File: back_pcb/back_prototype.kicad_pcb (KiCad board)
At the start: 2 copper layers, 40 x 100 mm, 84 parts, among them P1 EXPANSION_LEFT, P2 EXPANSION_BOTTOM, P3 EXPANSION_TOP, P4 USB_A, P5 AUDIO_CONN, P6 ATMEGA_HEADER, P7 EXPANSION_BOTTOM2, P8 CONN_01X02, Q1 IRLML6401, Q2 BSS138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

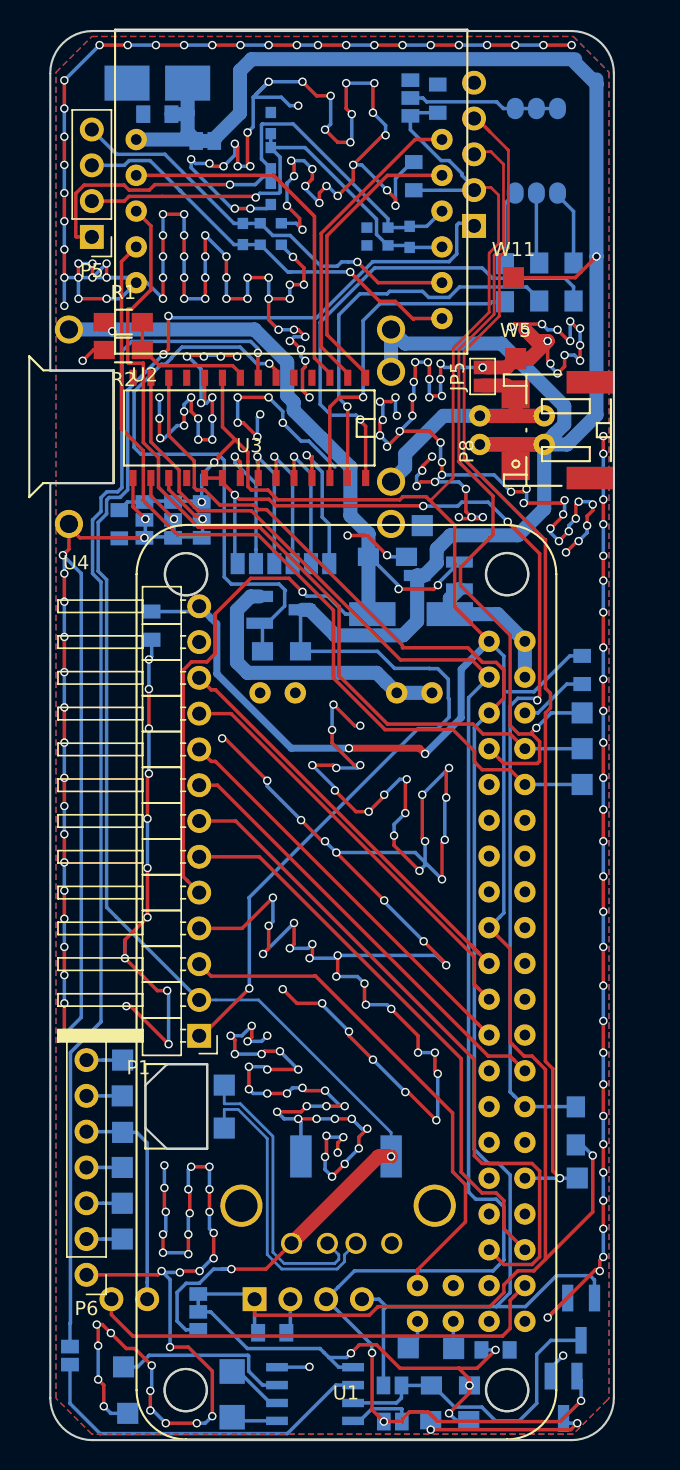
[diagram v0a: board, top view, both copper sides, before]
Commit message: Back board almost finished - lots of changes
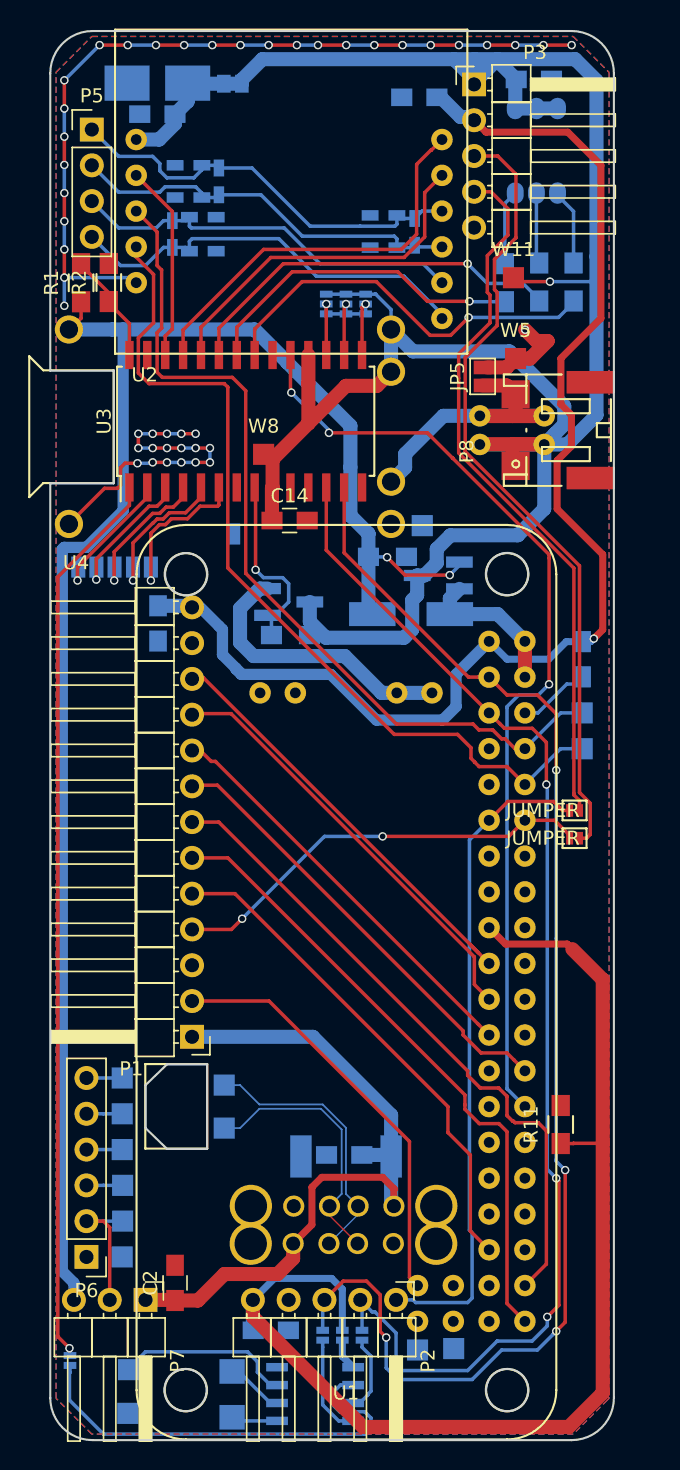
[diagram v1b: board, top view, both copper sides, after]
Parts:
- removed C7: 100nF, Capacitors_SMD:C_0805
- removed JP8: CA/CC, Connect:GS3
- removed Q2, Q3: BSS138, TO_SOT_Packages_SMD:SOT-23_Handsoldering
- removed R8, R9: 10K, Resistors_SMD:R_0805_HandSoldering
- removed W16: TEST_1P, Measurement_Points:Measurement_Point_Square-SMD-Pad_Small
- added C1: 100nF, Capacitors_SMD:C_0805_HandSoldering, B.Cu at (62.4, 119.8)
- added C2: 100nF, Capacitors_SMD:C_0805_HandSoldering, F.Cu at (50.4, 128.8)
- added JP11: JUMPER, common-footprints:GS2_SMALL, F.Cu at (79.1, 95.3)
- added JP12: JUMPER, common-footprints:GS2_SMALL, F.Cu at (79.1, 97.3)
- added P9: USB_A, footprints:USB_A, B.Cu at (65.9, 123.4)
- C13, C15, C25, C5, C6, C8: footprint Capacitors_SMD:C_0805 -> Capacitors_SMD:C_0805_HandSoldering
- C14: footprint Capacitors_SMD:C_0805 -> Capacitors_SMD:C_0805_HandSoldering; moved to F.Cu
- C16, C17, C18, C19, C20, C21, C22, C23, C24: footprint Capacitors_SMD:C_0603 -> Capacitors_SMD:C_0603_HandSoldering
- C4: value 10uF -> 100uF
- JP10, JP2, JP9: footprint Connect:GS2 -> common-footprints:GS2_SMALL
- JP3, JP4, JP6: footprint Connect:GS3 -> common-footprints:GS3_SMALL
- JP7: value 3V3/5V -> Jumper_NC_Small; footprint Connect:GS3 -> common-footprints:GS2_SMALL
- P2: footprint Pin_Headers:Pin_Header_Angled_1x04_Pitch2.54mm -> Pin_Headers:Pin_Header_Angled_1x05_Pitch2.54mm; moved to F.Cu
- P3, R11, W8: moved to F.Cu
- P4: footprint Connect:USB_A -> footprints:USB_A
- P6: footprint Pin_Headers:Pin_Header_Straight_1x07_Pitch2.54mm -> Pin_Headers:Pin_Header_Straight_1x06_Pitch2.54mm
- P7: footprint Pin_Headers:Pin_Header_Angled_1x02_Pitch2.54mm -> Pin_Headers:Pin_Header_Angled_1x03_Pitch2.54mm; moved to F.Cu
- P8: value CONN_01X02 -> JST
- U3: footprint SMD_Packages:SOIC-28 -> Housings_SOIC:SOIC-28W_7.5x17.9mm_Pitch1.27mm
- W12, W5, W6: value TEST_1P -> GND
- W27: value TEST_1P -> ATMEGA_VCC
- moved W7 52.9 mm to (48.6, 78.0), turned to 90 degrees
- moved W6 50.6 mm to (46.6, 127.0)
- moved W8 46.6 mm to (56.6, 70.0)
- moved JP3 21.9 mm to (63.9, 59.4)
- moved JP6 19.6 mm to (62.5, 59.4)
- moved JP4 17.7 mm to (61.1, 59.4)
- moved W23 12.6 mm to (47.6, 78.0)
- moved W24 12.6 mm to (49.2, 78.0)
- moved W22 12.6 mm to (46.0, 78.0)
- moved W21 12.6 mm to (44.4, 78.0)
- moved C14 12.1 mm to (58.5, 74.7), turned to 0 degrees
- moved W13 11.4 mm to (46.6, 114.3)
- moved JP7 10.3 mm to (62.2, 132.2), turned to 0 degrees
- moved P3 10.0 mm to (71.6, 43.8)
- moved P2 10.0 mm to (66.0, 130.0)
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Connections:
- C13 pad 1: +3V3 -> +BATT
- C14 pad 1: +3V3 -> +BATT
- C16 pad 2: MIC+ -> MIC-
- C17 pad 1: MIC+ -> MIC-
- C17 pad 2: MIC- -> MIC+
- C18 pad 1: MIC- -> MIC+
- C19 pad 2: SPK+ -> SPK-
- C20 pad 1: SPK+ -> SPK-
- C20 pad 2: SPK- -> SPK+
- C21 pad 1: SPK- -> SPK+
- C22 pad 2: MIC+ -> MIC-
- C23 pad 1: MIC+ -> MIC-
- C23 pad 2: MIC- -> MIC+
- C24 pad 1: MIC- -> MIC+
- D3 pad 1: Net-(D3-Pad1) -> +BATT
- JP2 pad 1: RTC_ALARM -> Net-(JP2-Pad1)
- JP2 pad 2: Net-(JP2-Pad2) -> RTC_ALARM
- JP3 pad 3: +3V3 -> +BATT
- JP4 pad 1: +3V3 -> +BATT
- JP6 pad 3: +3V3 -> +BATT
- JP7 pad 1: +3V3 -> Net-(JP7-Pad1)
- P1 pad 1: +BATT -> +5V
- P1 pad 2: +5V -> TV_OUT
- P1 pad 3: TV_OUT -> GND
- P1 pad 4: GND -> LH_GPIO_4
- P1 pad 5: VDD -> LH_GPIO_3
- P2 pad 1: +3V3 -> BH_GPIO_1
- P2 pad 2: GND -> SCL
- P2 pad 4: SCL -> GND
- P3 pad 1: +5V -> +BATT
- P5 pad 3: SPK- -> SPK+
- P5 pad 4: SPK+ -> SPK-
- P6 pad 2: ATMEGA_RST -> ATMEGA_ADC
- P6 pad 3: ATMEGA_RXD -> Net-(P6-Pad3)
- P6 pad 4: ATMEGA_TXD -> ATMEGA_RXD
- P6 pad 5: ATMEGA_ADC -> ATMEGA_TXD
- P6 pad 6: ATMEGA_GPIO -> ATMEGA_R_G
- P7 pad 1: BH_GPIO -> +5V
- U1 pad 11: (no net) -> BH_GPIO_1
- U1 pad 12: (no net) -> LH_GPIO_4
- U1 pad 32: IR_RX -> (no net)
- U1 pad 35: LH_GPIO_1 -> LH_GPIO_3
- U1 pad 36: LH_GPIO_2 -> (no net)
- U1 pad 38: BH_GPIO -> LH_GPIO_1
- U1 pad 40: (no net) -> LH_GPIO_2
- U1 pad 44: Net-(U1-Pad44) -> GND
- U1 pad 7: IR_TX -> (no net)
- U3 pad 1: SIM800_DTR -> RTC_ALARM
- U3 pad 18: (no net) -> +BATT
- U3 pad 2: SIM800_RING -> Net-(U3-Pad2)
- U3 pad 21: Net-(U3-Pad21) -> NOTIF_LED_R
- U3 pad 22: Net-(U3-Pad22) -> NOTIF_LED_B
- U3 pad 23: Net-(U3-Pad23) -> NOTIF_LED_G
- U3 pad 24: Net-(U3-Pad24) -> SIM800_DTR
- U3 pad 25: Net-(U3-Pad25) -> SIM800_RING
- U3 pad 26: NOTIF_LED_B -> SIM800_RST
- U3 pad 27: NOTIF_LED_G -> (no net)
- U3 pad 28: NOTIF_LED_R -> CHARGING_SENSE
- U3 pad 3: SIM800_RST -> Net-(U3-Pad3)
- U3 pad 4: (no net) -> Net-(U3-Pad4)
- U3 pad 5: (no net) -> Net-(U3-Pad5)
- U3 pad 6: DCDC_EN -> Net-(U3-Pad6)
- U3 pad 7: Net-(JP2-Pad2) -> Net-(U3-Pad7)
- U3 pad 8: CHARGING_SENSE -> DCDC_EN
- U3 pad 9: +3V3 -> +BATT
- U5 pad 5: +3V3 -> Net-(JP7-Pad1)
- U5 pad 6: RTC_ALARM -> Net-(JP2-Pad1)
- W13 pad 1: ATMEGA_RST -> ATMEGA_R_G
- W21 pad 1: Net-(U3-Pad21) -> Net-(U3-Pad2)
- W22 pad 1: Net-(U3-Pad22) -> Net-(U3-Pad3)
- W23 pad 1: Net-(U3-Pad23) -> Net-(U3-Pad4)
- W24 pad 1: Net-(U3-Pad24) -> Net-(U3-Pad5)
- W27 pad 1: Net-(P6-Pad7) -> Net-(P6-Pad3)
- W4 pad 1: Net-(U1-Pad44) -> GND
- W6 pad 1: IR_TX -> GND
- W7 pad 1: IR_RX -> Net-(U3-Pad6)
- W8 pad 1: ATMEGA_GPIO -> Net-(U3-Pad7)
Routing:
- net GND: track 778.0 -> 110.4 mm, vias 346 -> 48
- net Net-(JP2-Pad2): track 85.4 -> 0.00 mm, vias 1 -> 0
- net +3V3: track 249.1 -> 176.0 mm, vias 9 -> 1
- net +5V: track 122.6 -> 50.4 mm, vias 4 -> 0
- net BH_GPIO_1: track 0.00 -> 46.7 mm
- net RTC_ALARM: track 25.2 -> 64.1 mm, vias 0 -> 1
- net VDD: track 83.2 -> 120.2 mm, vias 4 -> 2
- net LH_GPIO_3: track 0.00 -> 35.8 mm
- net BH_GPIO: track 33.7 -> 0.00 mm
- net IR_RX: track 84.2 -> 50.8 mm, vias 1 -> 0
- net Net-(JP2-Pad1): track 0.00 -> 31.3 mm
- net LH_GPIO_4: track 0.00 -> 30.6 mm, vias 0 -> 2
- net DCDC_EN: track 42.0 -> 13.3 mm
- net SDA: track 121.5 -> 95.1 mm, vias 3 -> 4
- net SCL: track 108.6 -> 88.3 mm, vias 0 -> 3
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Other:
- net class Default: trace_width 0.1 -> 0.25

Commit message: Cleaning up ground planes
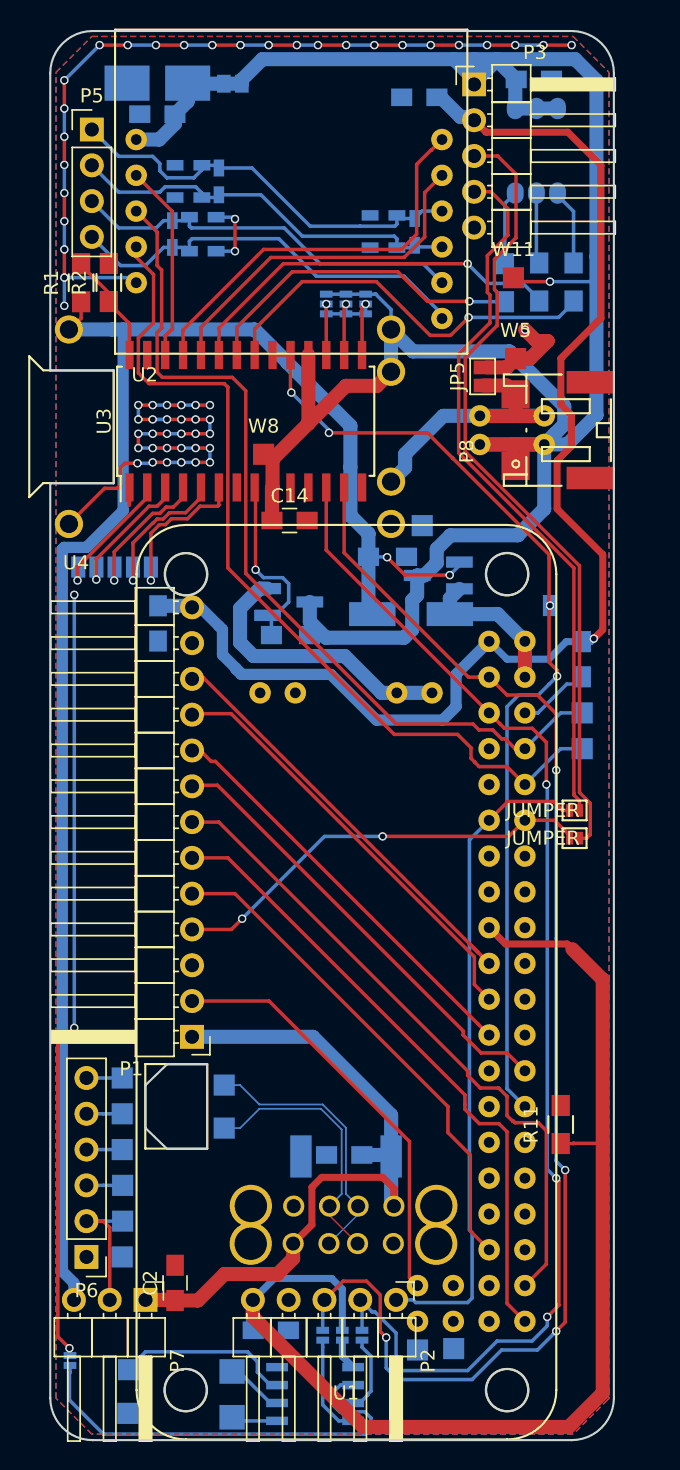
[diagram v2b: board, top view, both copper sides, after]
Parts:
- moved W28 23.0 mm to (77.6, 80.8)
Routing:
- net GND: track 110.4 -> 128.7 mm, vias 48 -> 63
- net RTC_ALARM: track 64.1 -> 56.1 mm, vias 1 -> 3
- net Net-(U3-Pad7): track 0.00 -> 5.59 mm
- net +BATT: track 171.6 -> 166.0 mm
- net MCP_INT: track 68.9 -> 69.6 mm, vias 3 -> 4
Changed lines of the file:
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@@
   (general
     (links 196)
-    (no_connects 18)
+    (no_connects 13)
     (area 41.424999 39.924999 81.575001 140.075001)
     (thickness 1.6)
     (drawings 22)
-    (tracks 832)
+    (tracks 875)
     (zones 0)
     (modules 82)
@@
     (36 B.SilkS user hide)
     (37 F.SilkS user hide)
-    (38 B.Mask user hide)
-    (39 F.Mask user hide)
+    (38 B.Mask user)
+    (39 F.Mask user)
     (40 Dwgs.User user hide)
     (41 Cmts.User user hide)
@@
   )
   (module Measurement_Points:Measurement_Point_Square-SMD-Pad_Small (layer B.Cu)
-    (at 55.083 75.692)
+    (at 77.562 80.772)
     (descr "Mesurement Point, Square, SMD Pad,  1.5mm x 1.5mm,")
     (tags "Mesurement Point Square SMD Pad 1.5x1.5mm")
@@
   (segment (start 70.612 46.101) (end 71.3486 46.101) (width 1) (layer B.Cu) (net 1))
   (segment (start 51.6928 81.2) (end 52.07 80.8228) (width 0.25) (layer B.Cu) (net 1))
+  (segment (start 51.816 66.548) (end 52.832 66.548) (width 0.25) (layer F.Cu) (net 2))
+  (via (at 52.832 66.548) (size 0.6) (drill 0.4) (layers F.Cu B.Cu) (net 2))
+  (segment (start 50.8 66.548) (end 51.816 66.548) (width 0.25) (layer B.Cu) (net 2))
+  (via (at 51.816 66.548) (size 0.6) (drill 0.4) (layers F.Cu B.Cu) (net 2))
+  (segment (start 49.784 66.548) (end 50.8 66.548) (width 0.25) (layer F.Cu) (net 2))
+  (via (at 50.8 66.548) (size 0.6) (drill 0.4) (layers F.Cu B.Cu) (net 2))
+  (segment (start 48.768 66.548) (end 49.784 66.548) (width 0.25) (layer B.Cu) (net 2))
+  (via (at 49.784 66.548) (size 0.6) (drill 0.4) (layers F.Cu B.Cu) (net 2))
+  (segment (start 47.752 66.548) (end 48.768 66.548) (width 0.25) (layer F.Cu) (net 2))
+  (via (at 48.768 66.548) (size 0.6) (drill 0.4) (layers F.Cu B.Cu) (net 2))
+  (segment (start 47.752 67.564) (end 47.752 66.548) (width 0.25) (layer B.Cu) (net 2))
+  (via (at 47.752 66.548) (size 0.6) (drill 0.4) (layers F.Cu B.Cu) (net 2))
+  (segment (start 48.768 67.564) (end 47.752 67.564) (width 0.25) (layer F.Cu) (net 2))
+  (via (at 47.752 67.564) (size 0.6) (drill 0.4) (layers F.Cu B.Cu) (net 2))
+  (segment (start 49.784 67.564) (end 48.768 67.564) (width 0.25) (layer B.Cu) (net 2))
+  (via (at 48.768 67.564) (size 0.6) (drill 0.4) (layers F.Cu B.Cu) (net 2))
+  (segment (start 50.8 67.564) (end 49.784 67.564) (width 0.25) (layer F.Cu) (net 2))
+  (via (at 49.784 67.564) (size 0.6) (drill 0.4) (layers F.Cu B.Cu) (net 2))
+  (via (at 50.8 67.564) (size 0.6) (drill 0.4) (layers F.Cu B.Cu) (net 2))
+  (segment (start 51.816 67.564) (end 50.8 67.564) (width 0.25) (layer F.Cu) (net 2))
+  (via (at 51.816 67.564) (size 0.6) (drill 0.4) (layers F.Cu B.Cu) (net 2))
+  (segment (start 52.832 67.564) (end 51.816 67.564) (width 0.25) (layer F.Cu) (net 2))
+  (segment (start 52.832 68.58) (end 52.832 67.564) (width 0.25) (layer B.Cu) (net 2))
+  (via (at 52.832 67.564) (size 0.6) (drill 0.4) (layers F.Cu B.Cu) (net 2))
+  (segment (start 51.816 68.58) (end 52.832 68.58) (width 0.25) (layer F.Cu) (net 2))
+  (via (at 52.832 68.58) (size 0.6) (drill 0.4) (layers F.Cu B.Cu) (net 2))
+  (segment (start 54.61 55.626) (end 53.274 55.626) (width 0.25) (layer B.Cu) (net 2))
+  (segment (start 54.61 53.34) (end 54.61 55.626) (width 0.25) (layer F.Cu) (net 2))
+  (via (at 54.61 55.626) (size 0.6) (drill 0.4) (layers F.Cu B.Cu) (net 2))
+  (segment (start 53.274 53.213) (end 54.483 53.213) (width 0.25) (layer B.Cu) (net 2))
+  (segment (start 54.483 53.213) (end 54.61 53.34) (width 0.25) (layer B.Cu) (net 2))
+  (via (at 54.61 53.34) (size 0.6) (drill 0.4) (layers F.Cu B.Cu) (net 2))
   (segment (start 50.8 68.58) (end 51.816 68.58) (width 0.25) (layer F.Cu) (net 2))
   (via (at 51.816 68.58) (size 0.6) (drill 0.4) (layers F.Cu B.Cu) (net 2))
@@
   (segment (start 64.684401 65.180799) (end 62.488201 65.180799) (width 1) (layer F.Cu) (net 16))
   (segment (start 62.488201 65.180799) (end 59.817 67.852) (width 1) (layer F.Cu) (net 16))
-  (segment (start 57.277 72.392) (end 57.277 70.392) (width 1) (layer F.Cu) (net 16))
-  (segment (start 57.277 70.392) (end 59.817 67.852) (width 1) (layer F.Cu) (net 16))
   (segment (start 59.817 67.852) (end 59.817 64.992) (width 1) (layer F.Cu) (net 16))
   (segment (start 59.817 64.992) (end 59.817 62.992) (width 1) (layer F.Cu) (net 16))
@@
   (segment (start 71.9836 69.342) (end 76.5556 69.342) (width 1) (layer B.Cu) (net 16))
   (segment (start 65.6844 61.1808) (end 65.6844 64.1808) (width 1) (layer B.Cu) (net 16))
+  (segment (start 43.2045 110.744) (end 43.2045 80.01) (width 0.25) (layer B.Cu) (net 17))
+  (via (at 43.2045 80.01) (size 0.6) (drill 0.4) (layers F.Cu B.Cu) (net 17))
+  (segment (start 42.037 112.014) (end 42.037 132.6515) (width 0.25) (layer F.Cu) (net 17))
+  (segment (start 42.037 112.014) (end 42.037 111.9115) (width 0.25) (layer F.Cu) (net 17))
+  (segment (start 42.037 111.9115) (end 43.2045 110.744) (width 0.25) (layer F.Cu) (net 17))
+  (via (at 43.2045 110.744) (size 0.6) (drill 0.4) (layers F.Cu B.Cu) (net 17))
   (segment (start 42.8625 133.477) (end 42.8625 133.9625) (width 0.25) (layer B.Cu) (net 17))
   (segment (start 42.8625 133.9625) (end 42.9 134) (width 0.25) (layer B.Cu) (net 17))
-  (segment (start 42.037 78.74) (end 42.037 132.6515) (width 0.25) (layer F.Cu) (net 17))
   (segment (start 42.037 132.6515) (end 42.8625 133.477) (width 0.25) (layer F.Cu) (net 17))
   (via (at 42.8625 133.477) (size 0.6) (drill 0.4) (layers F.Cu B.Cu) (net 17))
-  (segment (start 47.117 73.66) (end 42.037 78.74) (width 0.25) (layer F.Cu) (net 17))
   (segment (start 47.117 73.092) (end 47.117 73.66) (width 0.25) (layer F.Cu) (net 17))
   (segment (start 47.117 72.392) (end 47.117 73.092) (width 0.25) (layer F.Cu) (net 17))
@@
   (segment (start 75.184 93.472) (end 77.724 90.932) (width 0.25) (layer B.Cu) (net 37))
   (segment (start 77.724 90.932) (end 79.248 90.932) (width 0.25) (layer B.Cu) (net 37))
+  (segment (start 76.8985 84.792736) (end 76.8985 84.7725) (width 0.25) (layer F.Cu) (net 38))
+  (segment (start 76.8985 84.7725) (end 76.8985 81.026) (width 0.25) (layer F.Cu) (net 38))
+  (segment (start 77.47 85.7885) (end 77.47 85.364236) (width 0.25) (layer F.Cu) (net 38))
+  (segment (start 77.47 85.364236) (end 76.8985 84.792736) (width 0.25) (layer F.Cu) (net 38))
+  (segment (start 76.8985 86.36) (end 77.47 85.7885) (width 0.25) (layer B.Cu) (net 38))
+  (via (at 77.47 85.7885) (size 0.6) (drill 0.4) (layers F.Cu B.Cu) (net 38))
+  (segment (start 73.914 87.9475) (end 74.7395 87.122) (width 0.25) (layer B.Cu) (net 38))
+  (segment (start 75.184 116.332) (end 73.914 115.062) (width 0.25) (layer B.Cu) (net 38))
+  (segment (start 73.914 115.062) (end 73.914 87.9475) (width 0.25) (layer B.Cu) (net 38))
+  (segment (start 76.1365 87.122) (end 76.8985 86.36) (width 0.25) (layer B.Cu) (net 38))
+  (segment (start 74.7395 87.122) (end 76.1365 87.122) (width 0.25) (layer B.Cu) (net 38))
+  (segment (start 76.8985 81.026) (end 76.8985 77.4065) (width 0.25) (layer F.Cu) (net 38))
+  (segment (start 76.962 80.772) (end 76.962 80.9625) (width 0.25) (layer F.Cu) (net 38))
+  (segment (start 76.962 80.9625) (end 76.8985 81.026) (width 0.25) (layer F.Cu) (net 38))
+  (via (at 76.962 80.772) (size 0.6) (drill 0.4) (layers F.Cu B.Cu) (net 38))
   (segment (start 61.2775 68.5165) (end 68.2625 68.5165) (width 0.25) (layer F.Cu) (net 38))
   (segment (start 68.2625 68.5165) (end 70.0405 70.2945) (width 0.25) (layer F.Cu) (net 38))
@@
   (segment (start 76.8985 77.1525) (end 70.08499 70.33899) (width 0.25) (layer F.Cu) (net 38))
   (segment (start 76.8985 77.4065) (end 76.8985 77.1525) (width 0.25) (layer F.Cu) (net 38))
-  (segment (start 74.7395 87.122) (end 76.1365 87.122) (width 0.25) (layer B.Cu) (net 38))
-  (segment (start 76.1365 87.122) (end 76.8985 86.36) (width 0.25) (layer B.Cu) (net 38))
-  (via (at 76.8985 86.36) (size 0.6) (drill 0.4) (layers F.Cu B.Cu) (net 38))
-  (segment (start 73.914 115.062) (end 73.914 88.011) (width 0.25) (layer B.Cu) (net 38))
-  (segment (start 73.914 88.011) (end 73.914 87.9475) (width 0.25) (layer B.Cu) (net 38))
-  (segment (start 73.914 87.9475) (end 74.7395 87.122) (width 0.25) (layer B.Cu) (net 38))
-  (segment (start 75.184 116.332) (end 73.914 115.062) (width 0.25) (layer B.Cu) (net 38))
-  (segment (start 76.8985 86.36) (end 76.8985 77.4065) (width 0.25) (layer F.Cu) (net 38))
   (segment (start 57.277 62.992) (end 58.547 62.992) (width 0.25) (layer F.Cu) (net 38))
   (segment (start 57.592 138.6332) (end 54.662 138.6332) (width 0.25) (layer B.Cu) (net 39))
@@
   (segment (start 53.467 72.392) (end 53.467 73.642) (width 0.25) (layer F.Cu) (net 60))
   (segment (start 53.467 73.642) (end 53.3855 73.7235) (width 0.25) (layer F.Cu) (net 60))
+  (segment (start 57.277 72.392) (end 57.277 70.392) (width 1) (layer F.Cu) (net 61))
+  (segment (start 57.277 70.392) (end 59.817 67.852) (width 1) (layer F.Cu) (net 61))
   (segment (start 66.04 130.048) (end 67.242081 130.048) (width 0.25) (layer B.Cu) (net 62))
   (segment (start 67.242081 130.048) (end 67.432581 130.2385) (width 0.25) (layer B.Cu) (net 62))
@@
     (connect_pads (clearance 0.25))
     (min_thickness 0.2)
-    (fill yes (arc_segments 16) (thermal_gap 0.3) (thermal_bridge_width 0.508))
+    (fill yes (arc_segments 16) (thermal_gap 0.3) (thermal_bridge_width 0.25))
     (polygon
       (pts
@@
     (polygon
       (pts
-        (xy 47.625 64.77) (xy 55.245 64.77) (xy 55.245 70.485) (xy 47.625 70.485)
+        (xy 47.244 64.77) (xy 55.245 64.77) (xy 55.118 70.866) (xy 47.244 70.866)
       )
     )
